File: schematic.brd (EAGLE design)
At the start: 108.2 x 139.7 mm, 126 parts, among them IC1 AD8015, IC2 AD8015, IC3 AD8015, IC4 AD8015

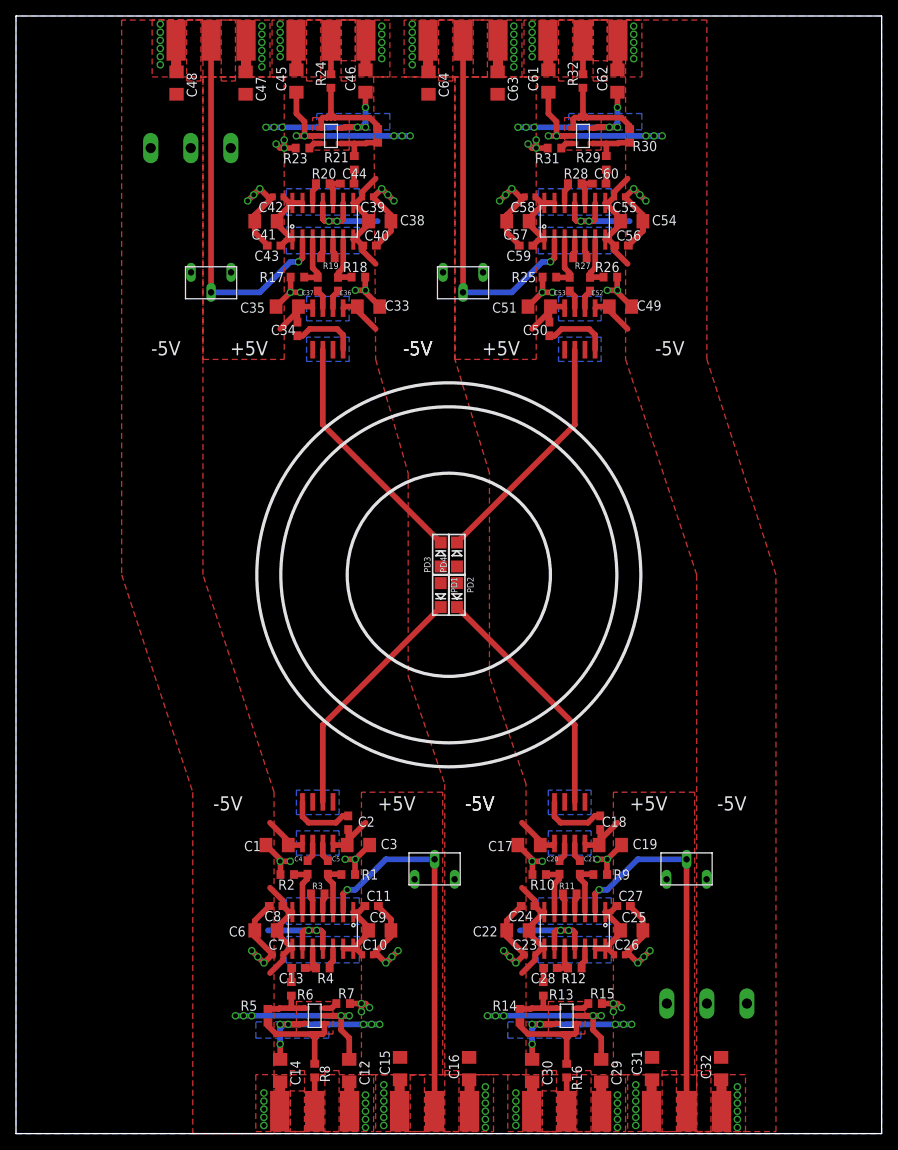
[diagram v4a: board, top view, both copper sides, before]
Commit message: Silkscreen updated for each channel fixed vias by connectors
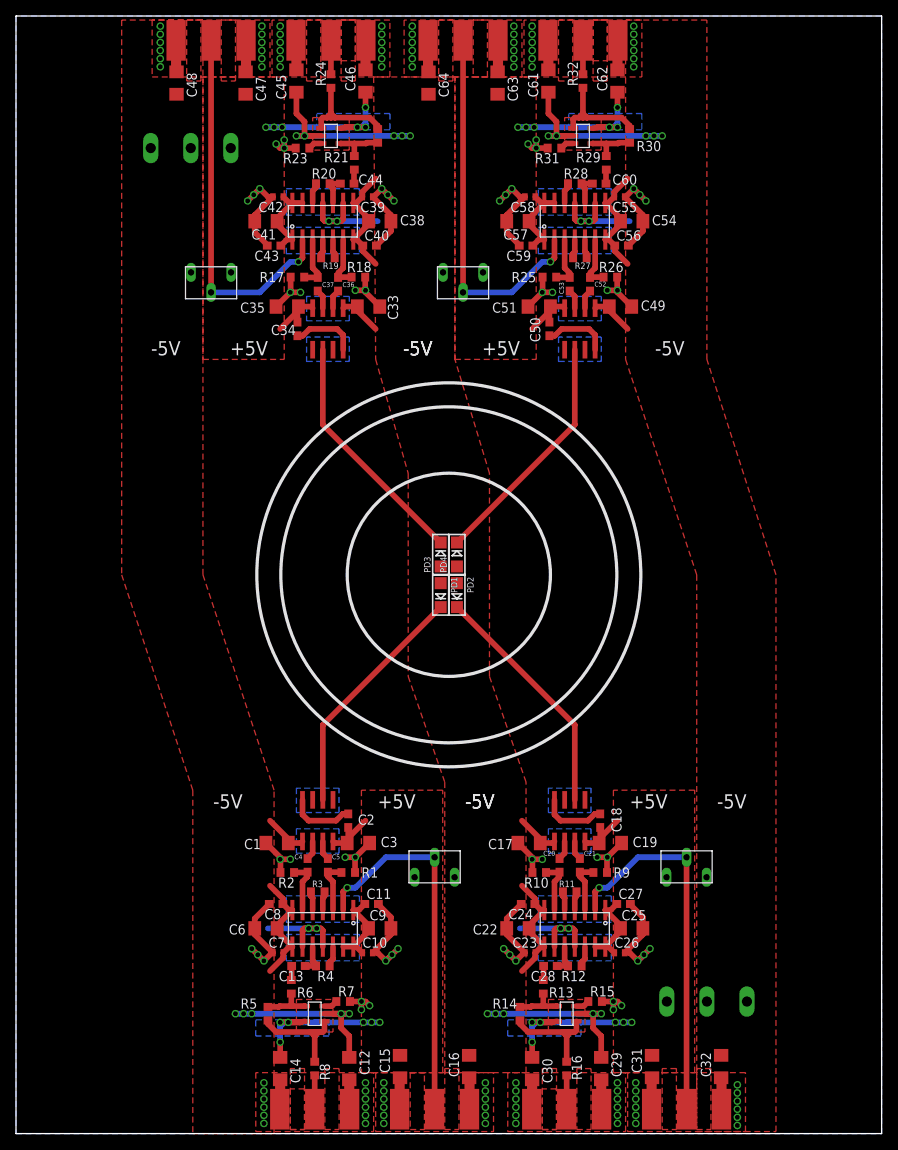
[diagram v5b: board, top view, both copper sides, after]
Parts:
- moved C1 0.25 mm to (32.6, 36.3)
- moved C17 0.25 mm to (64.1, 36.3)
- moved C19 0.25 mm to (74.3, 36.3)
- moved C3 0.25 mm to (42.8, 36.3)
- moved R1 0.25 mm to (41.5, 32.6)
- moved R10 0.25 mm to (65.4, 32.6)
- moved R2 0.25 mm to (33.9, 32.6)
- moved R9 0.25 mm to (73.0, 32.6)
- moved C10 0.25 mm to (43.9, 22.6)
- moved C11 0.25 mm to (44.5, 28.7)
- moved C22 0.25 mm to (62.7, 25.7)
- moved C23 0.25 mm to (64.3, 22.6)
- moved C24 0.25 mm to (64.0, 28.7)
- moved C25 0.25 mm to (77.0, 25.7)
- moved C26 0.25 mm to (75.4, 22.6)
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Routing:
- net GND: vias 148 -> 156

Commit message: Connected more power planes
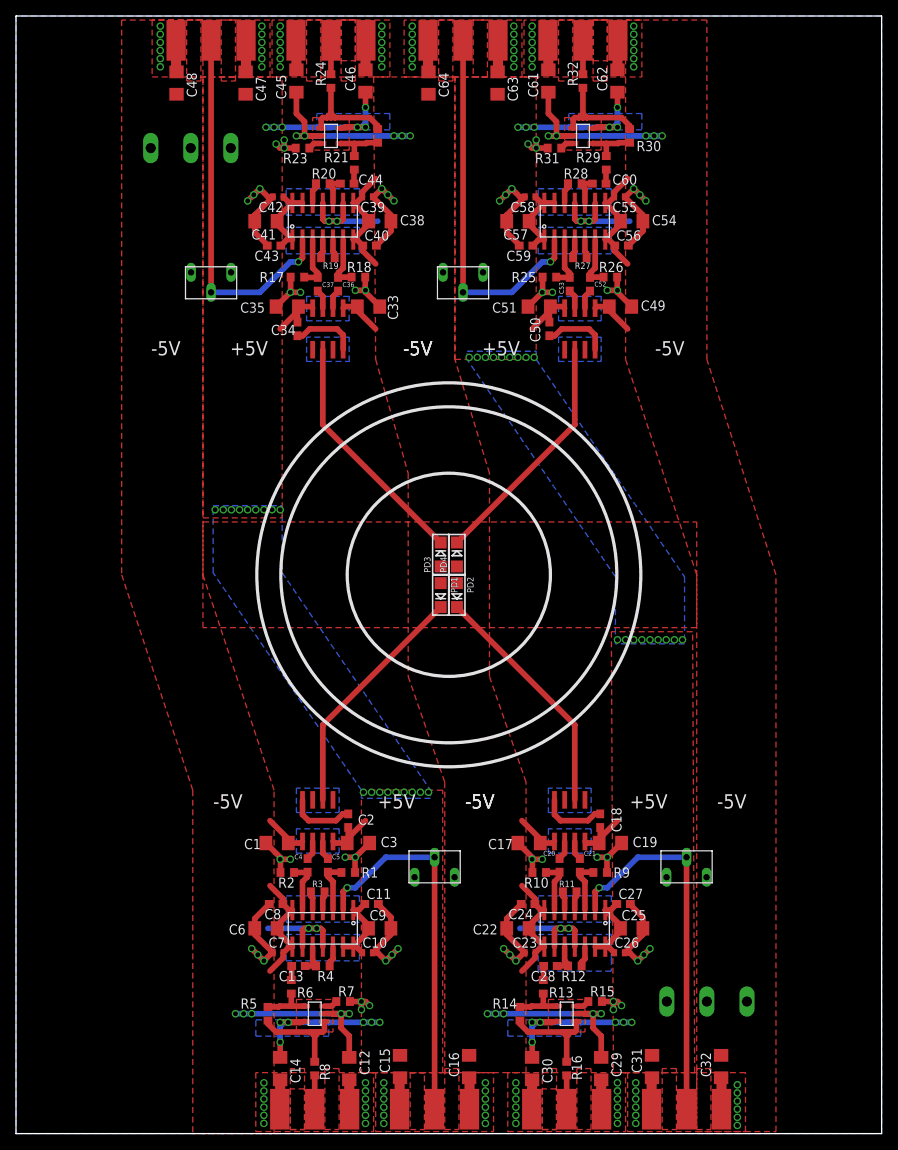
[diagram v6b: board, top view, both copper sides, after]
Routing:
- net +5V: vias 24 -> 60
- added copper zone on layer 16, net +5V
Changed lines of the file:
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@@
 <wire x1="48.26" y1="124.714" x2="49.276" y2="124.714" width="0.7112" layer="16"/>
 <contactref element="U$22" pad="-5"/>
-<wire x1="51.562" y1="129.918" x2="66.548" y2="130.172" width="0" layer="19" extent="1-1"/>
-<wire x1="20.066" y1="129.918" x2="35.052" y2="130.172" width="0" layer="19" extent="1-1"/>
-<wire x1="73.152" y1="9.528" x2="88.138" y2="9.782" width="0" layer="19" extent="1-1"/>
-<wire x1="53.086" y1="70.894" x2="44.958" y2="100.584" width="0" layer="19" extent="1-1"/>
+<polygon width="0.4064" layer="1" isolate="0.6096" rank="2">
+<vertex x="85.09" y="76.454"/>
+<vertex x="85.09" y="63.246"/>
+<vertex x="23.368" y="63.246"/>
+<vertex x="23.368" y="76.454"/>
+</polygon>
+<wire x1="35.052" y1="130.172" x2="20.066" y2="129.918" width="0" layer="19" extent="1-1"/>
+<wire x1="56.642" y1="9.782" x2="41.656" y2="9.528" width="0" layer="19" extent="1-1"/>
 </signal>
 <signal name="+5V">
@@
 <vertex x="74.676" y="7.62"/>
 <vertex x="84.836" y="7.62"/>
-<vertex x="84.836" y="42.926"/>
-<vertex x="74.676" y="42.926"/>
+<vertex x="84.582" y="62.738"/>
+<vertex x="74.422" y="62.738"/>
 </polygon>
 <wire x1="73.025" y1="36.452" x2="73.025" y2="35.941" width="0.7112" layer="1"/>
@@
 <contactref element="C47" pad="1"/>
 <polygon width="0.7112" layer="1" isolate="0.6096" rank="3">
-<vertex x="33.528" y="132.08"/>
+<vertex x="33.274" y="132.08"/>
 <vertex x="23.368" y="132.08"/>
-<vertex x="23.368" y="96.774"/>
-<vertex x="33.528" y="96.774"/>
+<vertex x="23.368" y="76.962"/>
+<vertex x="33.274" y="76.962"/>
 </polygon>
 <wire x1="35.179" y1="103.248" x2="35.179" y2="103.759" width="0.7112" layer="1"/>
@@
 <wire x1="75.1205" y1="126.238" x2="74.676" y2="125.7935" width="0.7112" layer="16"/>
 <contactref element="U$22" pad="+5V"/>
-<wire x1="43.688" y1="130.172" x2="60.198" y2="129.918" width="0" layer="19" extent="1-1"/>
-<wire x1="75.184" y1="39.116" x2="64.516" y2="100.584" width="0" layer="19" extent="1-1"/>
+<polygon width="0.7112" layer="16" isolate="0.6096">
+<vertex x="43.18" y="42.926"/>
+<vertex x="24.638" y="70.104"/>
+<vertex x="24.638" y="78.486"/>
+<vertex x="33.274" y="78.486"/>
+<vertex x="33.274" y="70.104"/>
+<vertex x="51.816" y="42.926"/>
+<vertex x="51.816" y="41.91"/>
+<vertex x="43.18" y="41.91"/>
+</polygon>
+<via x="43.434" y="42.672" extent="1-16" drill="0.6"/>
+<via x="44.45" y="42.672" extent="1-16" drill="0.6"/>
+<via x="45.466" y="42.672" extent="1-16" drill="0.6"/>
+<via x="46.482" y="42.672" extent="1-16" drill="0.6"/>
+<via x="47.498" y="42.672" extent="1-16" drill="0.6"/>
+<via x="48.514" y="42.672" extent="1-16" drill="0.6"/>
+<via x="49.53" y="42.672" extent="1-16" drill="0.6"/>
+<via x="50.546" y="42.672" extent="1-16" drill="0.6"/>
+<via x="51.562" y="42.672" extent="1-16" drill="0.6"/>
+<via x="24.892" y="77.978" extent="1-16" drill="0.6"/>
+<via x="25.908" y="77.978" extent="1-16" drill="0.6"/>
+<via x="26.924" y="77.978" extent="1-16" drill="0.6"/>
+<via x="27.94" y="77.978" extent="1-16" drill="0.6"/>
+<via x="28.956" y="77.978" extent="1-16" drill="0.6"/>
+<via x="29.972" y="77.978" extent="1-16" drill="0.6"/>
+<via x="30.988" y="77.978" extent="1-16" drill="0.6"/>
+<via x="32.004" y="77.978" extent="1-16" drill="0.6"/>
+<via x="33.02" y="77.978" extent="1-16" drill="0.6"/>
+<polygon width="0.7112" layer="16" isolate="0.6096">
+<vertex x="65.024" y="96.774"/>
+<vertex x="83.566" y="69.596"/>
+<vertex x="83.566" y="61.214"/>
+<vertex x="74.93" y="61.214"/>
+<vertex x="74.93" y="69.596"/>
+<vertex x="56.388" y="96.774"/>
+<vertex x="56.388" y="97.79"/>
+<vertex x="65.024" y="97.79"/>
+</polygon>
+<via x="56.642" y="97.028" extent="1-16" drill="0.6"/>
+<via x="57.658" y="97.028" extent="1-16" drill="0.6"/>
+<via x="58.674" y="97.028" extent="1-16" drill="0.6"/>
+<via x="59.69" y="97.028" extent="1-16" drill="0.6"/>
+<via x="60.706" y="97.028" extent="1-16" drill="0.6"/>
+<via x="61.722" y="97.028" extent="1-16" drill="0.6"/>
+<via x="62.738" y="97.028" extent="1-16" drill="0.6"/>
+<via x="63.754" y="97.028" extent="1-16" drill="0.6"/>
+<via x="64.77" y="97.028" extent="1-16" drill="0.6"/>
+<via x="83.312" y="61.722" extent="1-16" drill="0.6"/>
+<via x="82.296" y="61.722" extent="1-16" drill="0.6"/>
+<via x="81.28" y="61.722" extent="1-16" drill="0.6"/>
+<via x="80.264" y="61.722" extent="1-16" drill="0.6"/>
+<via x="79.248" y="61.722" extent="1-16" drill="0.6"/>
+<via x="78.232" y="61.722" extent="1-16" drill="0.6"/>
+<via x="77.216" y="61.722" extent="1-16" drill="0.6"/>
+<via x="76.2" y="61.722" extent="1-16" drill="0.6"/>
+<via x="75.184" y="61.722" extent="1-16" drill="0.6"/>
 <wire x1="48.006" y1="9.782" x2="64.516" y2="9.528" width="0" layer="19" extent="1-1"/>
 </signal>
@@
 </polygon>
 <polygon width="0" layer="16" pour="cutout">
-<vertex x="74.422" y="21.59"/>
-<vertex x="65.278" y="21.59"/>
+<vertex x="74.422" y="20.32"/>
+<vertex x="65.278" y="20.32"/>
 <vertex x="65.278" y="24.892"/>
 <vertex x="74.422" y="24.892"/>
+<vertex x="74.422" y="21.844"/>
 </polygon>
 <polygon width="0" layer="1" pour="cutout">

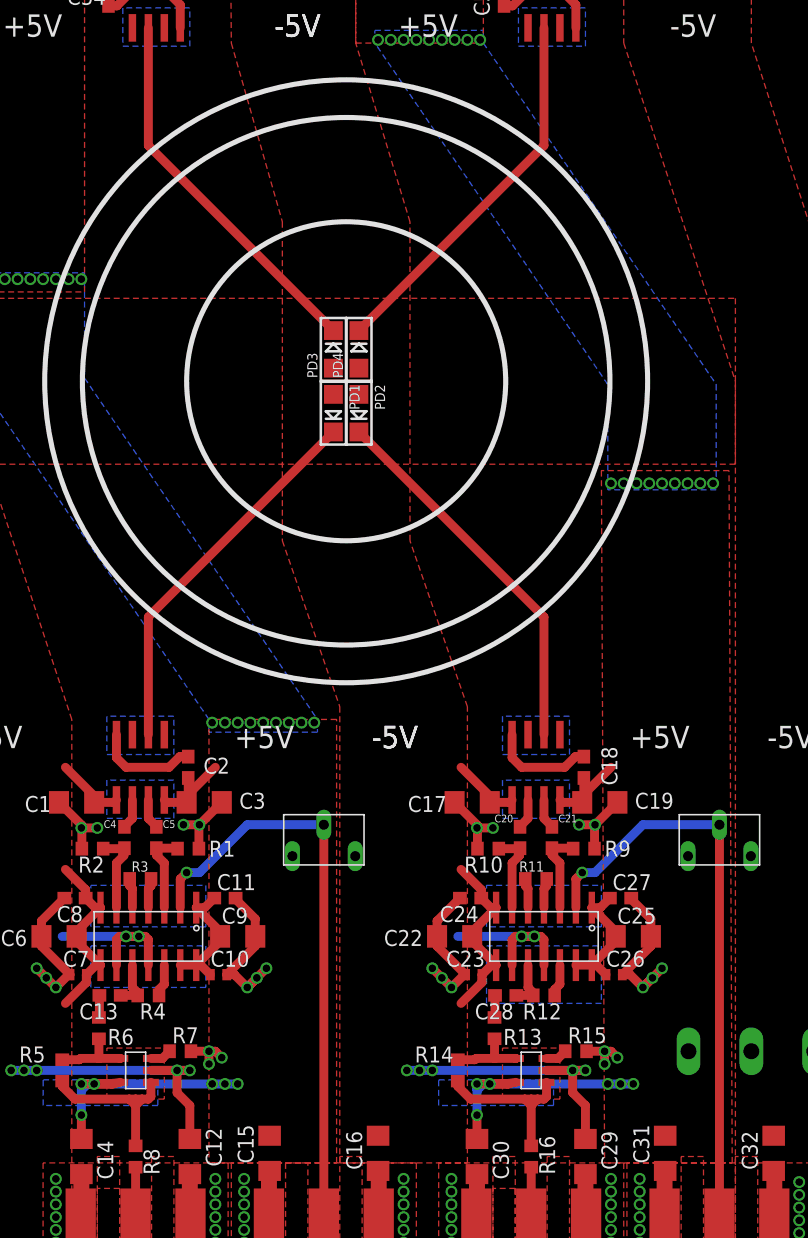
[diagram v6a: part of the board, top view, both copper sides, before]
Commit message: Wired all power planes, need to fine "unrouted" connections
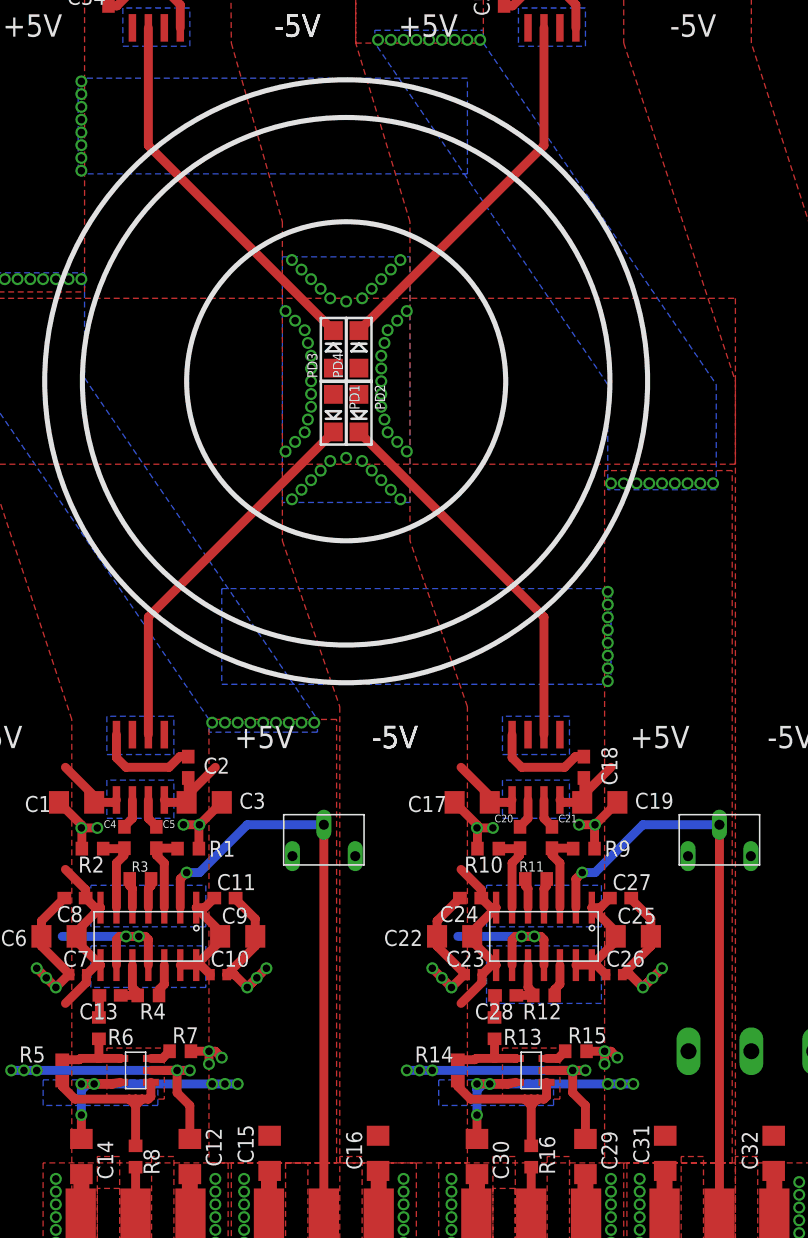
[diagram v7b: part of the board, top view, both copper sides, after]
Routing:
- net -5V: vias 20 -> 68
- net +5V: vias 60 -> 76
- added copper zone on layer 16, net -5V
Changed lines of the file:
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@@
 <vertex x="23.368" y="76.454"/>
 </polygon>
-<wire x1="35.052" y1="130.172" x2="20.066" y2="129.918" width="0" layer="19" extent="1-1"/>
-<wire x1="56.642" y1="9.782" x2="41.656" y2="9.528" width="0" layer="19" extent="1-1"/>
+<polygon width="0.7112" layer="16">
+<vertex x="49.022" y="79.756"/>
+<vertex x="59.182" y="79.756"/>
+<vertex x="59.182" y="60.198"/>
+<vertex x="49.022" y="60.198"/>
+</polygon>
+<via x="49.784" y="60.452" extent="1-16" drill="0.6"/>
+<via x="50.546" y="61.214" extent="1-16" drill="0.6"/>
+<via x="51.308" y="61.976" extent="1-16" drill="0.6"/>
+<via x="52.07" y="62.738" extent="1-16" drill="0.6"/>
+<via x="52.832" y="63.5" extent="1-16" drill="0.6"/>
+<via x="54.102" y="63.754" extent="1-16" drill="0.6"/>
+<via x="55.372" y="63.5" extent="1-16" drill="0.6"/>
+<via x="56.134" y="62.738" extent="1-16" drill="0.6"/>
+<via x="56.896" y="61.976" extent="1-16" drill="0.6"/>
+<via x="57.658" y="61.214" extent="1-16" drill="0.6"/>
+<via x="58.42" y="60.452" extent="1-16" drill="0.6"/>
+<via x="58.42" y="79.502" extent="1-16" drill="0.6"/>
+<via x="57.658" y="78.74" extent="1-16" drill="0.6"/>
+<via x="56.896" y="77.978" extent="1-16" drill="0.6"/>
+<via x="56.134" y="77.216" extent="1-16" drill="0.6"/>
+<via x="55.372" y="76.454" extent="1-16" drill="0.6"/>
+<via x="54.102" y="76.2" extent="1-16" drill="0.6"/>
+<via x="52.832" y="76.454" extent="1-16" drill="0.6"/>
+<via x="52.07" y="77.216" extent="1-16" drill="0.6"/>
+<via x="51.308" y="77.978" extent="1-16" drill="0.6"/>
+<via x="50.546" y="78.74" extent="1-16" drill="0.6"/>
+<via x="49.784" y="79.502" extent="1-16" drill="0.6"/>
+<via x="49.276" y="75.438" extent="1-16" drill="0.6"/>
+<via x="50.038" y="74.676" extent="1-16" drill="0.6"/>
+<via x="50.8" y="73.914" extent="1-16" drill="0.6"/>
+<via x="51.054" y="72.898" extent="1-16" drill="0.6"/>
+<via x="51.308" y="71.882" extent="1-16" drill="0.6"/>
+<via x="51.308" y="70.866" extent="1-16" drill="0.6"/>
+<via x="51.308" y="69.85" extent="1-16" drill="0.6"/>
+<via x="51.308" y="68.834" extent="1-16" drill="0.6"/>
+<via x="51.308" y="67.818" extent="1-16" drill="0.6"/>
+<via x="51.054" y="66.802" extent="1-16" drill="0.6"/>
+<via x="50.8" y="65.786" extent="1-16" drill="0.6"/>
+<via x="50.038" y="65.024" extent="1-16" drill="0.6"/>
+<via x="49.276" y="64.262" extent="1-16" drill="0.6"/>
+<via x="58.928" y="64.262" extent="1-16" drill="0.6"/>
+<via x="58.166" y="65.024" extent="1-16" drill="0.6"/>
+<via x="57.404" y="65.786" extent="1-16" drill="0.6"/>
+<via x="57.15" y="66.802" extent="1-16" drill="0.6"/>
+<via x="56.896" y="67.818" extent="1-16" drill="0.6"/>
+<via x="56.896" y="68.834" extent="1-16" drill="0.6"/>
+<via x="56.896" y="69.85" extent="1-16" drill="0.6"/>
+<via x="56.896" y="70.866" extent="1-16" drill="0.6"/>
+<via x="56.896" y="71.882" extent="1-16" drill="0.6"/>
+<via x="57.15" y="72.898" extent="1-16" drill="0.6"/>
+<via x="57.404" y="73.914" extent="1-16" drill="0.6"/>
+<via x="58.166" y="74.676" extent="1-16" drill="0.6"/>
+<via x="58.928" y="75.438" extent="1-16" drill="0.6"/>
 </signal>
 <signal name="+5V">
@@
 <vertex x="74.676" y="7.62"/>
 <vertex x="84.836" y="7.62"/>
-<vertex x="84.582" y="62.738"/>
-<vertex x="74.422" y="62.738"/>
+<vertex x="84.836" y="62.738"/>
+<vertex x="74.676" y="62.738"/>
 </polygon>
 <wire x1="73.025" y1="36.452" x2="73.025" y2="35.941" width="0.7112" layer="1"/>
@@
 <via x="76.2" y="61.722" extent="1-16" drill="0.6"/>
 <via x="75.184" y="61.722" extent="1-16" drill="0.6"/>
-<wire x1="48.006" y1="9.782" x2="64.516" y2="9.528" width="0" layer="19" extent="1-1"/>
+<polygon width="0.7112" layer="16">
+<vertex x="32.766" y="93.98"/>
+<vertex x="32.766" y="86.36"/>
+<vertex x="63.754" y="86.36"/>
+<vertex x="63.754" y="93.98"/>
+</polygon>
+<via x="33.02" y="86.614" extent="1-16" drill="0.6"/>
+<via x="33.02" y="87.63" extent="1-16" drill="0.6"/>
+<via x="33.02" y="88.646" extent="1-16" drill="0.6"/>
+<via x="33.02" y="89.662" extent="1-16" drill="0.6"/>
+<via x="33.02" y="90.678" extent="1-16" drill="0.6"/>
+<via x="33.02" y="91.694" extent="1-16" drill="0.6"/>
+<via x="33.02" y="92.71" extent="1-16" drill="0.6"/>
+<via x="33.02" y="93.726" extent="1-16" drill="0.6"/>
+<polygon width="0.7112" layer="16">
+<vertex x="75.184" y="45.72"/>
+<vertex x="75.184" y="53.34"/>
+<vertex x="44.196" y="53.34"/>
+<vertex x="44.196" y="45.72"/>
+</polygon>
+<via x="74.93" y="53.086" extent="1-16" drill="0.6"/>
+<via x="74.93" y="52.07" extent="1-16" drill="0.6"/>
+<via x="74.93" y="51.054" extent="1-16" drill="0.6"/>
+<via x="74.93" y="50.038" extent="1-16" drill="0.6"/>
+<via x="74.93" y="49.022" extent="1-16" drill="0.6"/>
+<via x="74.93" y="48.006" extent="1-16" drill="0.6"/>
+<via x="74.93" y="46.99" extent="1-16" drill="0.6"/>
+<via x="74.93" y="45.974" extent="1-16" drill="0.6"/>
 </signal>
 <signal name="N$3">
